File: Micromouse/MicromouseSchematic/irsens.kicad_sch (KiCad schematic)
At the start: 28 parts, among them J6 IR_1, J7 IR_2, J8 IR_3, J9 IR_4, Q2 DMN3065LW-7, Q3 DMN3065LW-7, Q4 DMN3065LW-7, Q5 DMN3065LW-7

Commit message: added some stuff
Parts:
- A1, A2, A3, A4: footprint SFH_3015_FA:XDCR_SFH_3015_FA -> SFH_3015_FA_FOOTPRINT:SFH_3015_FA; Availability (none) -> In Stock; Check_prices (none) -> https://www.snapeda.com/parts/SFH%203015%20FA/Osram/view-pa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; Description_1 (none) -> Phototransistors 870nm Side View 1206 (3216 Metric); MF (none) -> OSRAM Opto; MP (none) -> SFH 3015 FA; Package (none) -> 1206 Osram Opto; Price (none) -> None; SnapEDA_Link (none) -> https://www.snapeda.com/parts/SFH%203015%20FA/Osram/view-pa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
- J6, J7, J8, J9: footprint mushak_mount_footprint:IR_SLAVE_V_04 -> (none); symbol Connector:Conn_01x04_Male -> Connector:Conn_01x04_Pin
- Q2, Q3, Q4, Q5: footprint Package_TO_SOT_SMD:SOT-323_SC-70 -> DMN3065LW-7_FOOTPRINT:DMN3065LW-7; symbol Device:Q_NMOS_DGS -> Simulation_SPICE:NMOS

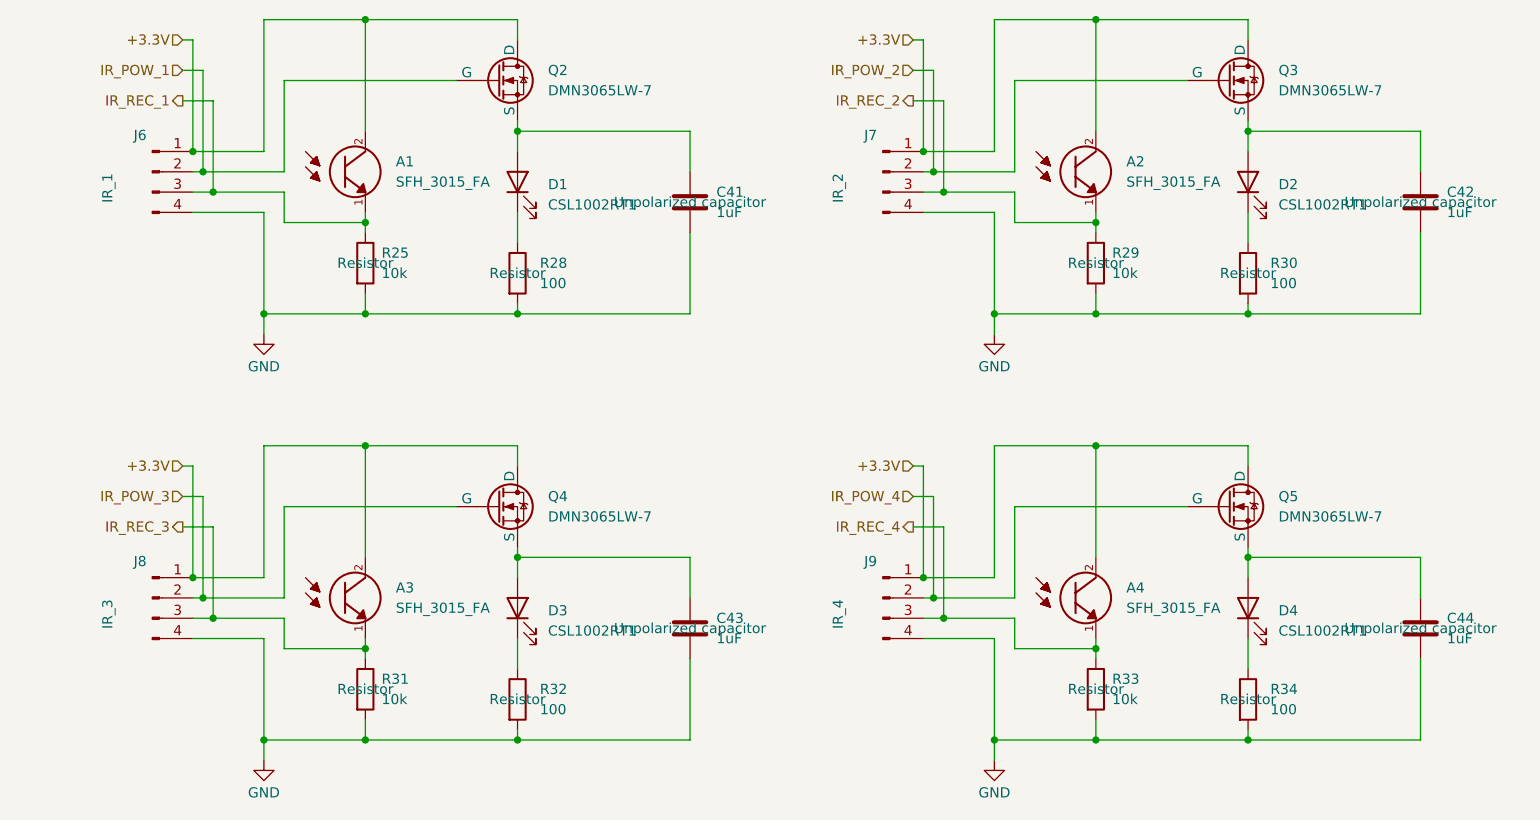
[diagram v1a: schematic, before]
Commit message: Micromouse KiCad: MP6550 libs in project, fp-lib paths, schematic updates
Move MP6550G-Z symbol and legacy footprints into MicromouseSchematic, add
MP6550G-Z.pretty with MP6550_MNP footprint, and point fp-lib-table at the
project-local MM_MP6550G-Z library.

Replace old absolute footprint paths with this repo’s Micromouse tree and
MM_* library names. Update root schematic and IMU/IR/motor/TOF/regulator
subsheets; add empty bluethooth.kicad_sch hierarchical sheet. Extend KiCad
project BOM field configuration; refresh fp-info-cache. Drop schematic lock
file; include dated schematic backup zip.
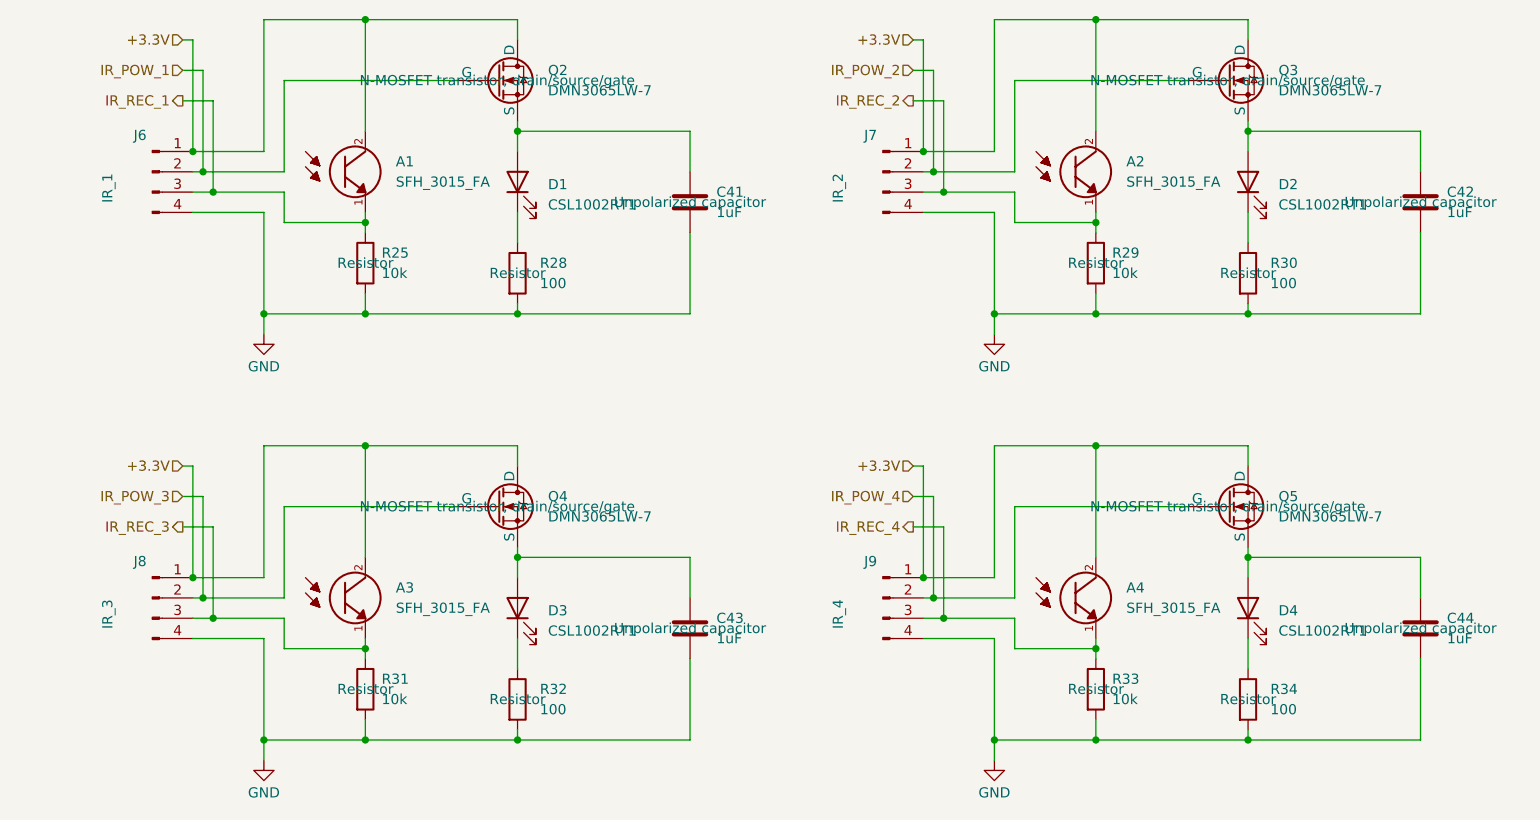
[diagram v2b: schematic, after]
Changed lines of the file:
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@@
 			)
 		)
-		(property "Datasheet" "~"
+		(property "Datasheet" "https://ngspice.sourceforge.io/docs/ngspice-html-manual/manual.xhtml#cha_MOSFETs"
 			(at 187.96 97.79 0)
 			(effects
@@
 			)
 		)
-		(property "Description" ""
+		(property "Description" "N-MOSFET transistor, drain/source/gate"
 			(at 187.96 97.79 0)
 			(effects
@@
 			)
 		)
-		(property "Datasheet" "~"
+		(property "Datasheet" "https://ngspice.sourceforge.io/docs/ngspice-html-manual/manual.xhtml#cha_MOSFETs"
 			(at 187.96 44.45 0)
 			(effects
@@
 			)
 		)
-		(property "Description" ""
+		(property "Description" "N-MOSFET transistor, drain/source/gate"
 			(at 187.96 44.45 0)
 			(effects
@@
 			)
 		)
-		(property "Datasheet" "~"
+		(property "Datasheet" "https://ngspice.sourceforge.io/docs/ngspice-html-manual/manual.xhtml#cha_MOSFETs"
 			(at 96.52 97.79 0)
 			(effects
@@
 			)
 		)
-		(property "Description" ""
+		(property "Description" "N-MOSFET transistor, drain/source/gate"
 			(at 96.52 97.79 0)
 			(effects
@@
 			)
 		)
-		(property "Datasheet" "~"
+		(property "Datasheet" "https://ngspice.sourceforge.io/docs/ngspice-html-manual/manual.xhtml#cha_MOSFETs"
 			(at 96.52 44.45 0)
 			(effects
@@
 			)
 		)
-		(property "Description" ""
+		(property "Description" "N-MOSFET transistor, drain/source/gate"
 			(at 96.52 44.45 0)
 			(effects

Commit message: Micromouse KiCad: STM32-centric routing; ERC errors 23→6; backups and gitignore
Body:
Connected almost all STM32 signals; ERC down to 6

Rework root schematic plus motor driver, IMU/magnetometer, IR sensor, and TOF
subsheets so the bulk of signals reach the STM32. KiCad ERC is not fully clean
yet, but major nets are in place: errors dropped from 23 to 6 while many
previously unconnected signals were wired.

Add 2026-04-08 schematic backup zips. Extend .gitignore for macOS .DS_Store
paths. Update MicromouseSchematic.kicad_prl.
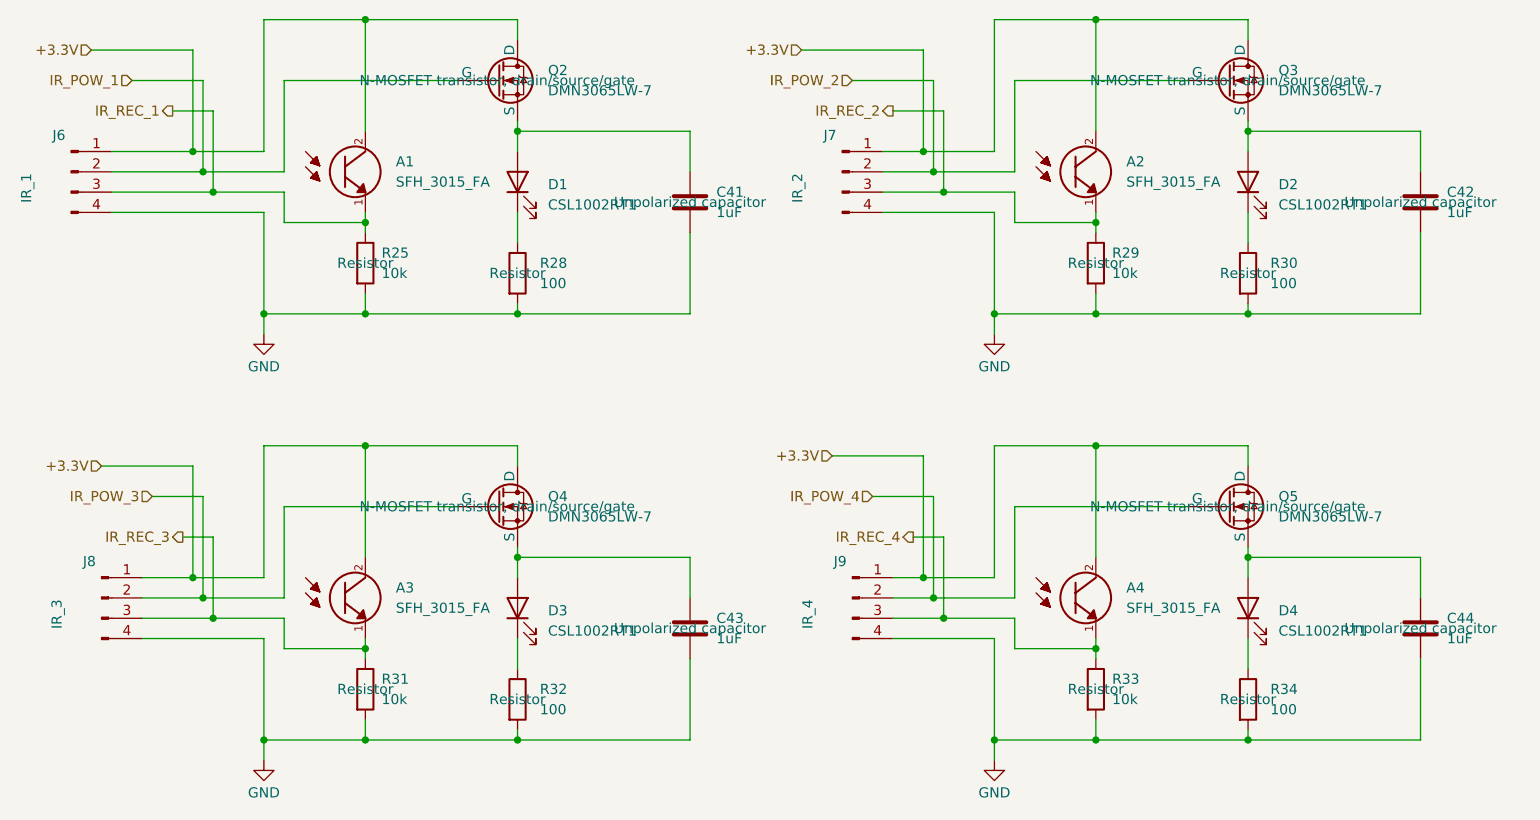
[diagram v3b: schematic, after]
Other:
- moved on the sheet: J6, J7, J8, J9

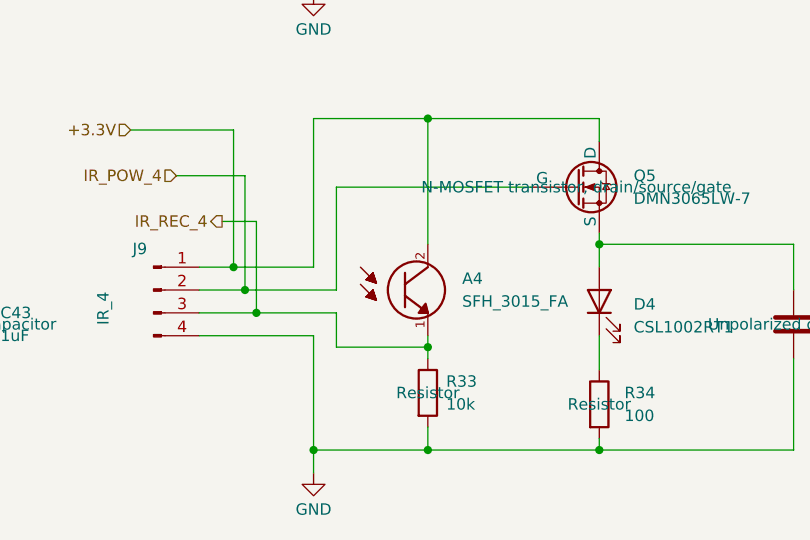
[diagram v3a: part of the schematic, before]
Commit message: Micromouse KiCad: MP6550 layout, schematic updates; ERC clean, warnings ~5–6
Relocate MP6550G-Z symbol and footprint trees from MicromouseSchematic into
Micromouse/MP6550G-Z and refresh sym-lib-table (portable ${KIPRJMOD} paths
where applicable, MP6550 at new location).

Update root schematic plus IMU, IR, motor driver, and TOF subsheets. KiCad
ERC: all errors resolved (previously 6 remaining after earlier bring-up).
Warnings reduced from roughly 35–40+ down to about 5–6.

Add MicromouseSchematic-2026-04-11_212024.zip backup.
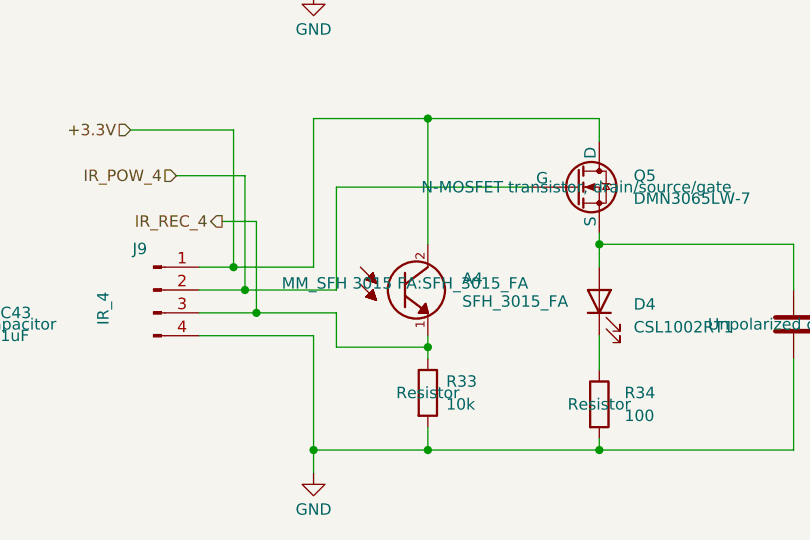
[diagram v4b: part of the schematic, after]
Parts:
- A1, A2, A3, A4: footprint SFH_3015_FA_FOOTPRINT:SFH_3015_FA -> MM_SFH 3015 FA:SFH_3015_FA
- Q2, Q3, Q4, Q5: footprint DMN3065LW-7_FOOTPRINT:DMN3065LW-7 -> MM_DMN3065LW-7:DMN3065LW-7
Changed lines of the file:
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@@
 			)
 		)
-		(property "Footprint" "SFH_3015_FA_FOOTPRINT:SFH_3015_FA"
+		(property "Footprint" "MM_SFH 3015 FA:SFH_3015_FA"
 			(at 77.47 55.88 0)
 			(effects
@@
 			)
 		)
-		(property "Footprint" "SFH_3015_FA_FOOTPRINT:SFH_3015_FA"
+		(property "Footprint" "MM_SFH 3015 FA:SFH_3015_FA"
 			(at 168.91 55.88 0)
 			(effects
@@
 			)
 		)
-		(property "Footprint" "DMN3065LW-7_FOOTPRINT:DMN3065LW-7"
+		(property "Footprint" "MM_DMN3065LW-7:DMN3065LW-7"
 			(at 193.04 95.25 0)
 			(effects
@@
 			)
 		)
-		(property "Footprint" "SFH_3015_FA_FOOTPRINT:SFH_3015_FA"
+		(property "Footprint" "MM_SFH 3015 FA:SFH_3015_FA"
 			(at 168.91 109.22 0)
 			(effects
@@
 				)
 				(justify bottom)
-				(hide yes)
 			)
 		)
@@
 			)
 		)
-		(property "Footprint" "DMN3065LW-7_FOOTPRINT:DMN3065LW-7"
+		(property "Footprint" "MM_DMN3065LW-7:DMN3065LW-7"
 			(at 193.04 41.91 0)
 			(effects
@@
 			)
 		)
-		(property "Footprint" "SFH_3015_FA_FOOTPRINT:SFH_3015_FA"
+		(property "Footprint" "MM_SFH 3015 FA:SFH_3015_FA"
 			(at 77.47 109.22 0)
 			(effects
@@
 			)
 		)
-		(property "Footprint" "DMN3065LW-7_FOOTPRINT:DMN3065LW-7"
+		(property "Footprint" "MM_DMN3065LW-7:DMN3065LW-7"
 			(at 101.6 95.25 0)
 			(effects
@@
 			)
 		)
-		(property "Footprint" "DMN3065LW-7_FOOTPRINT:DMN3065LW-7"
+		(property "Footprint" "MM_DMN3065LW-7:DMN3065LW-7"
 			(at 101.6 41.91 0)
 			(effects

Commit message: assigned capacitor footprints. still have to figure out rest
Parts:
- D1: footprint (none) -> Capacitor_SMD:C_0603_1608Metric
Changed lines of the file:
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@@
 			)
 		)
-		(property "Footprint" ""
+		(property "Footprint" "Capacitor_SMD:C_0603_1608Metric"
 			(at 99.06 57.15 0)
 			(effects

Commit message: added resistors, must need to add capacitors
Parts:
- C41, C42, C43, C44, D1: footprint Capacitor_SMD:C_0603_1608Metric -> (none)
- R25, R29, R31, R33: footprint Resistor_SMD:R_0402_1005Metric -> Resistor_SMD:R_0603_1608Metric
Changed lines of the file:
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@@
 			)
 		)
-		(property "Footprint" "Capacitor_SMD:C_0603_1608Metric"
+		(property "Footprint" ""
 			(at 121.6152 116.84 0)
 			(effects
@@
 			)
 		)
-		(property "Footprint" "Capacitor_SMD:C_0603_1608Metric"
+		(property "Footprint" ""
 			(at 213.0552 116.84 0)
 			(effects
@@
 			)
 		)
-		(property "Footprint" "Capacitor_SMD:C_0603_1608Metric"
+		(property "Footprint" ""
 			(at 99.06 57.15 0)
 			(effects
@@
 			)
 		)
-		(property "Footprint" "Capacitor_SMD:C_0603_1608Metric"
+		(property "Footprint" ""
 			(at 121.6152 63.5 0)
 			(effects
@@
 			)
 		)
-		(property "Footprint" "Resistor_SMD:R_0402_1005Metric"
+		(property "Footprint" "Resistor_SMD:R_0603_1608Metric"
 			(at 169.672 120.65 90)
 			(effects
@@
 			)
 		)
-		(property "Footprint" "Resistor_SMD:R_0402_1005Metric"
+		(property "Footprint" "Resistor_SMD:R_0603_1608Metric"
 			(at 169.672 67.31 90)
 			(effects
@@
 			)
 		)
-		(property "Footprint" "Resistor_SMD:R_0402_1005Metric"
+		(property "Footprint" "Resistor_SMD:R_0603_1608Metric"
 			(at 78.232 67.31 90)
 			(effects
@@
 			)
 		)
-		(property "Footprint" "Resistor_SMD:R_0402_1005Metric"
+		(property "Footprint" "Resistor_SMD:R_0603_1608Metric"
 			(at 78.232 120.65 90)
 			(effects
@@
 			)
 		)
-		(property "Footprint" "Capacitor_SMD:C_0603_1608Metric"
+		(property "Footprint" ""
 			(at 213.0552 63.5 0)
 			(effects
